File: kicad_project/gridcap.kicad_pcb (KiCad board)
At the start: 2 copper layers, 68 parts

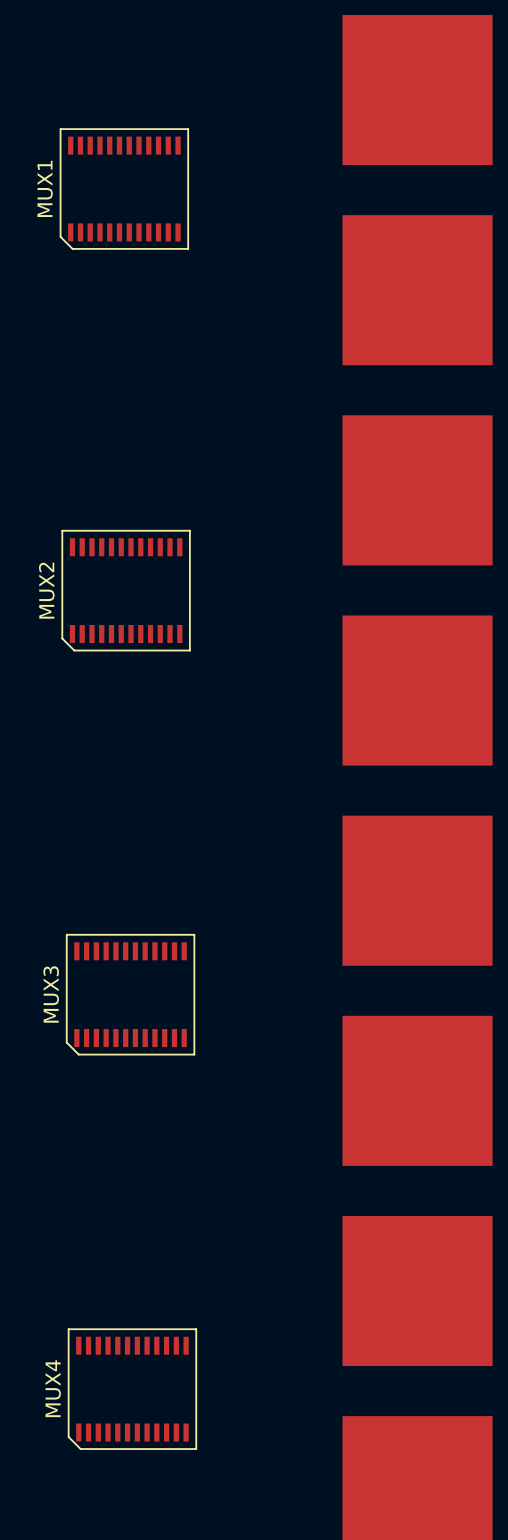
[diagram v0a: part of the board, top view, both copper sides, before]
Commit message: Fix pad pin number
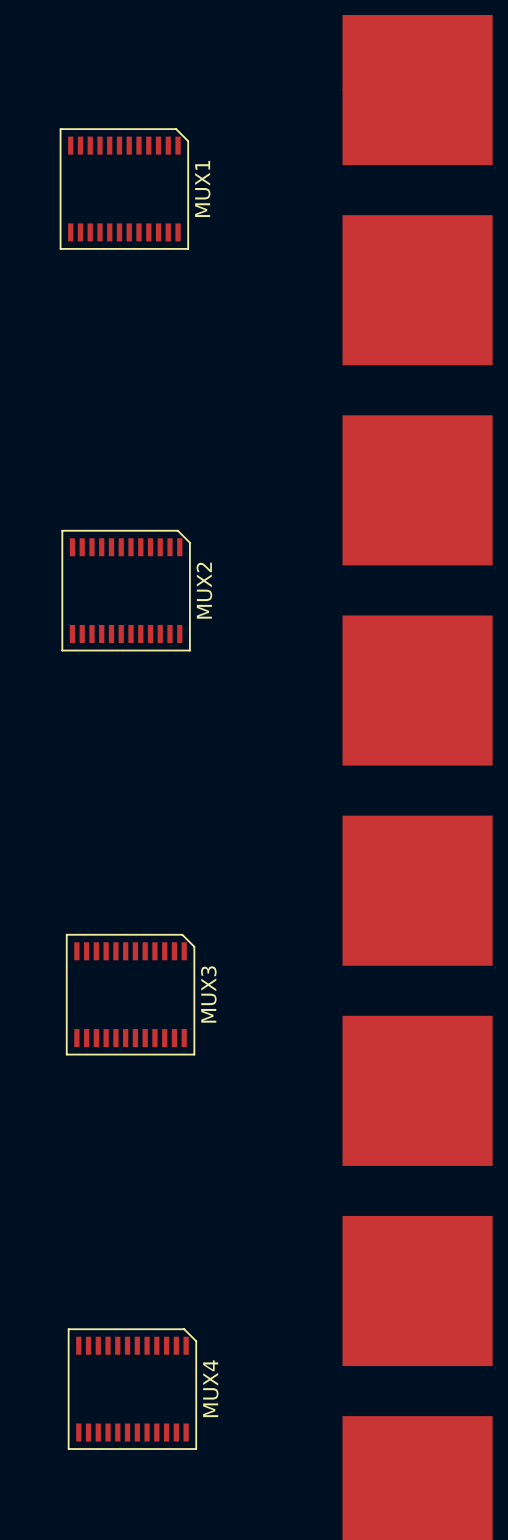
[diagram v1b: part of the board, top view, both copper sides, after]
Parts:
- turned MUX1 to 180 degrees
- turned MUX2 to 180 degrees
- turned MUX3 to 180 degrees
- turned MUX4 to 180 degrees
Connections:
- PAD1 pad 1: (no net) -> Net-(MUX1-Y7)
- PAD10 pad 1: (no net) -> Net-(MUX1-Y9)
- PAD11 pad 1: (no net) -> Net-(MUX1-Y10)
- PAD12 pad 1: (no net) -> Net-(MUX1-Y11)
- PAD13 pad 1: (no net) -> Net-(MUX1-Y12)
- PAD14 pad 1: (no net) -> Net-(MUX1-Y13)
- PAD15 pad 1: (no net) -> Net-(MUX1-Y14)
- PAD16 pad 1: (no net) -> Net-(MUX1-Y15)
- PAD17 pad 1: (no net) -> Net-(MUX2-Y7)
- PAD18 pad 1: (no net) -> Net-(MUX2-Y8)
- PAD19 pad 1: (no net) -> Net-(MUX2-Y6)
- PAD2 pad 1: (no net) -> Net-(MUX1-Y6)
- PAD20 pad 1: (no net) -> Net-(MUX2-Y9)
- PAD21 pad 1: (no net) -> Net-(MUX2-Y5)
- PAD22 pad 1: (no net) -> Net-(MUX2-Y10)
- PAD23 pad 1: (no net) -> Net-(MUX2-Y4)
- PAD24 pad 1: (no net) -> Net-(MUX2-Y11)
- PAD25 pad 1: (no net) -> Net-(MUX2-Y3)
- PAD26 pad 1: (no net) -> Net-(MUX2-Y12)
- PAD27 pad 1: (no net) -> Net-(MUX2-Y2)
- PAD28 pad 1: (no net) -> Net-(MUX2-Y13)
- PAD29 pad 1: (no net) -> Net-(MUX2-Y1)
- PAD3 pad 1: (no net) -> Net-(MUX1-Y5)
- PAD30 pad 1: (no net) -> Net-(MUX2-Y14)
- PAD31 pad 1: (no net) -> Net-(MUX2-Y0)
- PAD32 pad 1: (no net) -> Net-(MUX2-Y15)
- PAD33 pad 1: (no net) -> Net-(MUX3-Y7)
- PAD34 pad 1: (no net) -> Net-(MUX3-Y8)
- PAD35 pad 1: (no net) -> Net-(MUX3-Y6)
- PAD36 pad 1: (no net) -> Net-(MUX3-Y9)
- PAD37 pad 1: (no net) -> Net-(MUX3-Y5)
- PAD38 pad 1: (no net) -> Net-(MUX3-Y10)
- PAD39 pad 1: (no net) -> Net-(MUX3-Y4)
- PAD4 pad 1: (no net) -> Net-(MUX1-Y4)
- PAD40 pad 1: (no net) -> Net-(MUX3-Y11)
- PAD41 pad 1: (no net) -> Net-(MUX3-Y3)
- PAD42 pad 1: (no net) -> Net-(MUX3-Y12)
- PAD43 pad 1: (no net) -> Net-(MUX3-Y2)
- PAD44 pad 1: (no net) -> Net-(MUX3-Y13)
- PAD45 pad 1: (no net) -> Net-(MUX3-Y1)
- PAD46 pad 1: (no net) -> Net-(MUX3-Y14)
- PAD47 pad 1: (no net) -> Net-(MUX3-Y0)
- PAD48 pad 1: (no net) -> Net-(MUX3-Y15)
- PAD49 pad 1: (no net) -> Net-(MUX4-Y7)
- PAD5 pad 1: (no net) -> Net-(MUX1-Y3)
- PAD50 pad 1: (no net) -> Net-(MUX4-Y8)
- PAD51 pad 1: (no net) -> Net-(MUX4-Y6)
- PAD52 pad 1: (no net) -> Net-(MUX4-Y9)
- PAD53 pad 1: (no net) -> Net-(MUX4-Y5)
- PAD54 pad 1: (no net) -> Net-(MUX4-Y10)
- PAD55 pad 1: (no net) -> Net-(MUX4-Y4)
- PAD56 pad 1: (no net) -> Net-(MUX4-Y11)
- PAD57 pad 1: (no net) -> Net-(MUX4-Y3)
- PAD58 pad 1: (no net) -> Net-(MUX4-Y12)
- PAD59 pad 1: (no net) -> Net-(MUX4-Y2)
- PAD6 pad 1: (no net) -> Net-(MUX1-Y2)
- PAD60 pad 1: (no net) -> Net-(MUX4-Y13)
- PAD61 pad 1: (no net) -> Net-(MUX4-Y1)
- PAD62 pad 1: (no net) -> Net-(MUX4-Y14)
- PAD63 pad 1: (no net) -> Net-(MUX4-Y0)
- PAD64 pad 1: (no net) -> Net-(MUX4-Y15)
- PAD7 pad 1: (no net) -> Net-(MUX1-Y1)
- PAD8 pad 1: (no net) -> Net-(MUX1-Y0)
- PAD9 pad 1: (no net) -> Net-(MUX1-Y8)
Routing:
- net Net-(MUX1-Y7): track 0.00 -> 5.00 mm

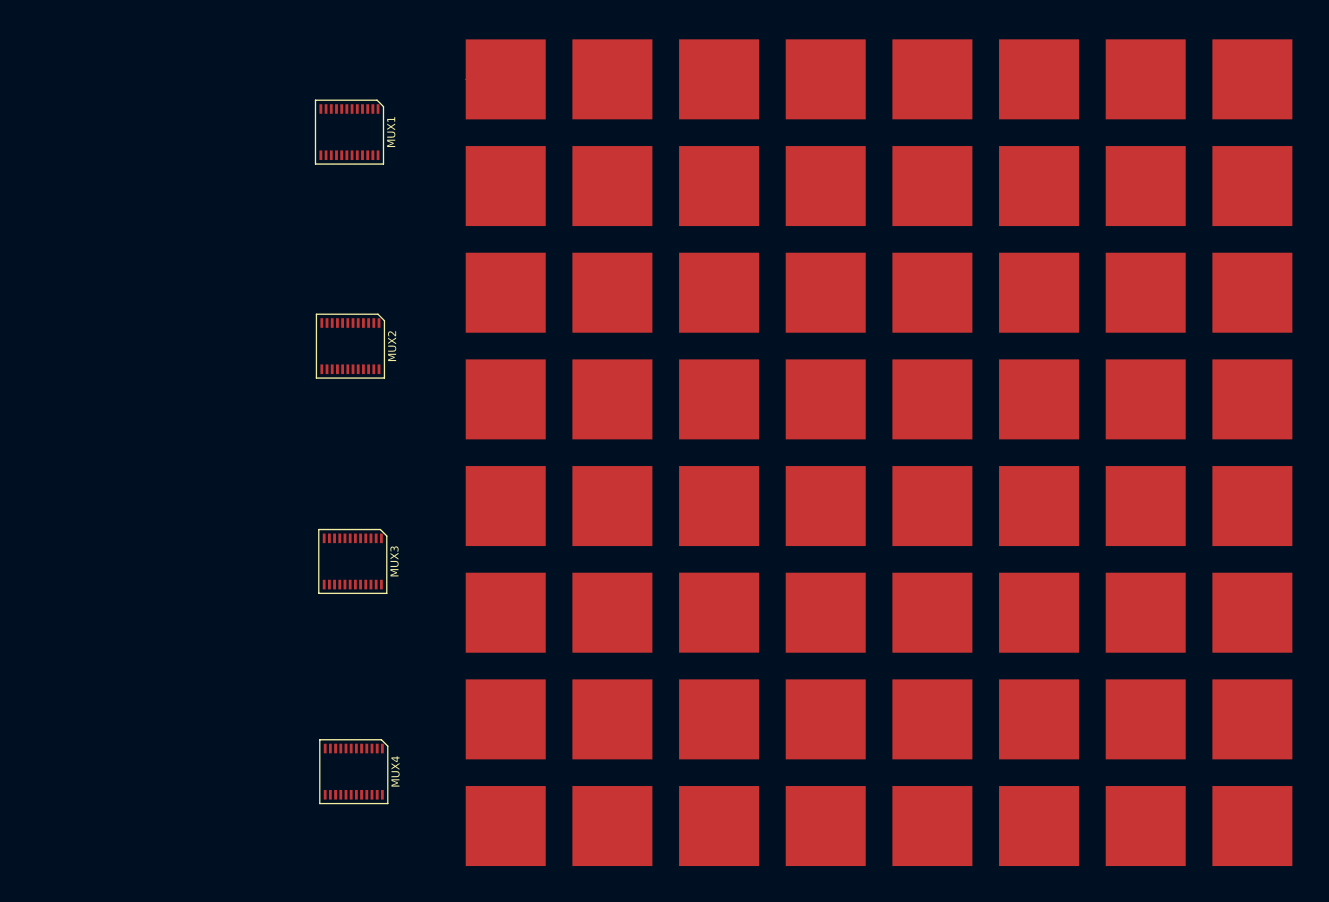
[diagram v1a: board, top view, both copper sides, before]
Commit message: Begin rewiring pads and muxes
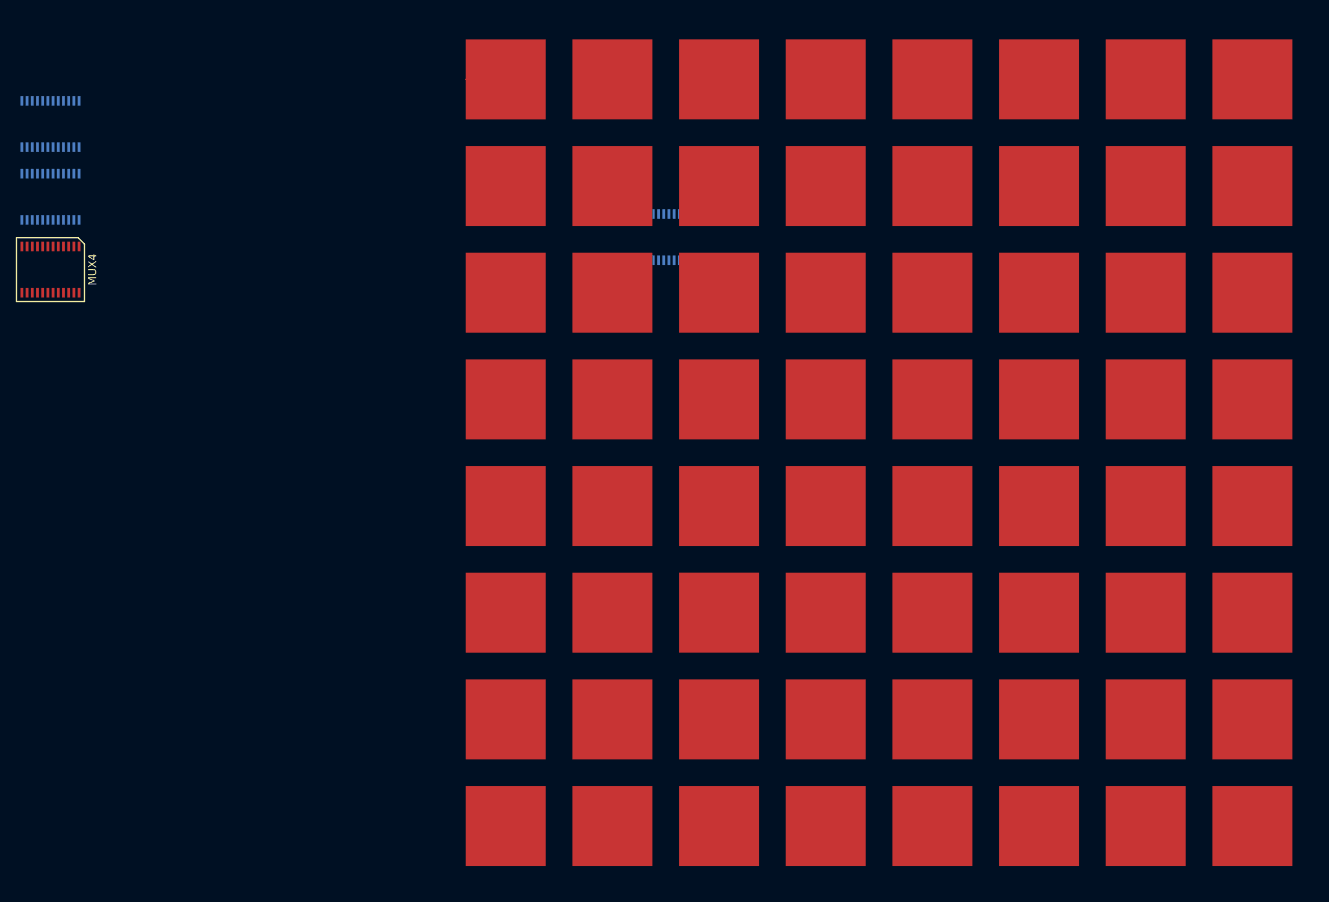
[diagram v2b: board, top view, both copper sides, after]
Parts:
- MUX1, MUX2, MUX3: moved to B.Cu
- moved MUX4 73.3 mm to (108.2, 77.1)
- moved MUX3 59.2 mm to (108.2, 68.0), turned to 0 degrees
- moved MUX2 46.7 mm to (108.2, 58.9), turned to 0 degrees
- moved MUX1 41.7 mm to (185.2, 73.1), turned to 0 degrees
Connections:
- MUX1 pad 12: (no net) -> GND
- MUX1 pad 24: (no net) -> unconnected-(MUX1-Vcc-Pad24)
- MUX2 pad 12: (no net) -> GND
- MUX2 pad 16: Net-(MUX2-Y15) -> unconnected-(MUX2-Y15-Pad16)
- MUX2 pad 17: Net-(MUX2-Y14) -> unconnected-(MUX2-Y14-Pad17)
- MUX2 pad 18: Net-(MUX2-Y13) -> unconnected-(MUX2-Y13-Pad18)
- MUX2 pad 19: Net-(MUX2-Y12) -> unconnected-(MUX2-Y12-Pad19)
- MUX2 pad 2: Net-(MUX2-Y7) -> unconnected-(MUX2-Y7-Pad2)
- MUX2 pad 20: Net-(MUX2-Y11) -> unconnected-(MUX2-Y11-Pad20)
- MUX2 pad 21: Net-(MUX2-Y10) -> unconnected-(MUX2-Y10-Pad21)
- MUX2 pad 22: Net-(MUX2-Y9) -> unconnected-(MUX2-Y9-Pad22)
- MUX2 pad 23: Net-(MUX2-Y8) -> unconnected-(MUX2-Y8-Pad23)
- MUX2 pad 24: (no net) -> unconnected-(MUX2-Vcc-Pad24)
- MUX2 pad 3: Net-(MUX2-Y6) -> unconnected-(MUX2-Y6-Pad3)
- MUX2 pad 4: Net-(MUX2-Y5) -> unconnected-(MUX2-Y5-Pad4)
- MUX2 pad 5: Net-(MUX2-Y4) -> unconnected-(MUX2-Y4-Pad5)
- MUX2 pad 6: Net-(MUX2-Y3) -> unconnected-(MUX2-Y3-Pad6)
- MUX2 pad 7: Net-(MUX2-Y2) -> unconnected-(MUX2-Y2-Pad7)
- MUX2 pad 8: Net-(MUX2-Y1) -> unconnected-(MUX2-Y1-Pad8)
- MUX2 pad 9: Net-(MUX2-Y0) -> unconnected-(MUX2-Y0-Pad9)
- MUX3 pad 12: (no net) -> GND
- MUX3 pad 16: Net-(MUX3-Y15) -> unconnected-(MUX3-Y15-Pad16)
- MUX3 pad 17: Net-(MUX3-Y14) -> unconnected-(MUX3-Y14-Pad17)
- MUX3 pad 18: Net-(MUX3-Y13) -> unconnected-(MUX3-Y13-Pad18)
- MUX3 pad 19: Net-(MUX3-Y12) -> unconnected-(MUX3-Y12-Pad19)
- MUX3 pad 2: Net-(MUX3-Y7) -> unconnected-(MUX3-Y7-Pad2)
- MUX3 pad 20: Net-(MUX3-Y11) -> unconnected-(MUX3-Y11-Pad20)
- MUX3 pad 21: Net-(MUX3-Y10) -> unconnected-(MUX3-Y10-Pad21)
- MUX3 pad 22: Net-(MUX3-Y9) -> unconnected-(MUX3-Y9-Pad22)
- MUX3 pad 23: Net-(MUX3-Y8) -> unconnected-(MUX3-Y8-Pad23)
- MUX3 pad 24: (no net) -> unconnected-(MUX3-Vcc-Pad24)
- MUX3 pad 3: Net-(MUX3-Y6) -> unconnected-(MUX3-Y6-Pad3)
- MUX3 pad 4: Net-(MUX3-Y5) -> unconnected-(MUX3-Y5-Pad4)
- MUX3 pad 5: Net-(MUX3-Y4) -> unconnected-(MUX3-Y4-Pad5)
- MUX3 pad 6: Net-(MUX3-Y3) -> unconnected-(MUX3-Y3-Pad6)
- MUX3 pad 7: Net-(MUX3-Y2) -> unconnected-(MUX3-Y2-Pad7)
- MUX3 pad 8: Net-(MUX3-Y1) -> unconnected-(MUX3-Y1-Pad8)
- MUX3 pad 9: Net-(MUX3-Y0) -> unconnected-(MUX3-Y0-Pad9)
- MUX4 pad 12: (no net) -> GND
- MUX4 pad 16: Net-(MUX4-Y15) -> unconnected-(MUX4-Y15-Pad16)
- MUX4 pad 17: Net-(MUX4-Y14) -> unconnected-(MUX4-Y14-Pad17)
- MUX4 pad 18: Net-(MUX4-Y13) -> unconnected-(MUX4-Y13-Pad18)
- MUX4 pad 19: Net-(MUX4-Y12) -> unconnected-(MUX4-Y12-Pad19)
- MUX4 pad 2: Net-(MUX4-Y7) -> unconnected-(MUX4-Y7-Pad2)
- MUX4 pad 20: Net-(MUX4-Y11) -> unconnected-(MUX4-Y11-Pad20)
- MUX4 pad 21: Net-(MUX4-Y10) -> unconnected-(MUX4-Y10-Pad21)
- MUX4 pad 22: Net-(MUX4-Y9) -> unconnected-(MUX4-Y9-Pad22)
- MUX4 pad 23: Net-(MUX4-Y8) -> unconnected-(MUX4-Y8-Pad23)
- MUX4 pad 24: (no net) -> unconnected-(MUX4-Vcc-Pad24)
- MUX4 pad 3: Net-(MUX4-Y6) -> unconnected-(MUX4-Y6-Pad3)
- MUX4 pad 4: Net-(MUX4-Y5) -> unconnected-(MUX4-Y5-Pad4)
- MUX4 pad 5: Net-(MUX4-Y4) -> unconnected-(MUX4-Y4-Pad5)
- MUX4 pad 6: Net-(MUX4-Y3) -> unconnected-(MUX4-Y3-Pad6)
- MUX4 pad 7: Net-(MUX4-Y2) -> unconnected-(MUX4-Y2-Pad7)
- MUX4 pad 8: Net-(MUX4-Y1) -> unconnected-(MUX4-Y1-Pad8)
- MUX4 pad 9: Net-(MUX4-Y0) -> unconnected-(MUX4-Y0-Pad9)
- PAD1 pad 1: Net-(MUX1-Y7) -> Net-(MUX1-Y6)
- PAD10 pad 1: Net-(MUX1-Y9) -> Net-(MUX1-Y5)
- PAD11 pad 1: Net-(MUX1-Y10) -> Net-(MUX1-Y2)
- PAD12 pad 1: Net-(MUX1-Y11) -> Net-(MUX1-Y0)
- PAD13 pad 1: Net-(MUX1-Y12) -> unconnected-(PAD13-Pad1)
- PAD14 pad 1: Net-(MUX1-Y13) -> unconnected-(PAD14-Pad1)
- PAD15 pad 1: Net-(MUX1-Y14) -> unconnected-(PAD15-Pad1)
- PAD16 pad 1: Net-(MUX1-Y15) -> unconnected-(PAD16-Pad1)
- PAD17 pad 1: Net-(MUX2-Y7) -> Net-(MUX1-Y8)
- PAD18 pad 1: Net-(MUX2-Y8) -> Net-(MUX1-Y10)
- PAD19 pad 1: Net-(MUX2-Y6) -> Net-(MUX1-Y13)
- PAD2 pad 1: Net-(MUX1-Y6) -> Net-(MUX1-Y4)
- PAD20 pad 1: Net-(MUX2-Y9) -> Net-(MUX1-Y15)
- PAD21 pad 1: Net-(MUX2-Y5) -> unconnected-(PAD21-Pad1)
- PAD22 pad 1: Net-(MUX2-Y10) -> unconnected-(PAD22-Pad1)
- PAD23 pad 1: Net-(MUX2-Y4) -> unconnected-(PAD23-Pad1)
- PAD24 pad 1: Net-(MUX2-Y11) -> unconnected-(PAD24-Pad1)
- PAD25 pad 1: Net-(MUX2-Y3) -> Net-(MUX1-Y9)
- PAD26 pad 1: Net-(MUX2-Y12) -> Net-(MUX1-Y11)
- PAD27 pad 1: Net-(MUX2-Y2) -> Net-(MUX1-Y12)
- PAD28 pad 1: Net-(MUX2-Y13) -> Net-(MUX1-Y14)
- PAD29 pad 1: Net-(MUX2-Y1) -> unconnected-(PAD29-Pad1)
- PAD3 pad 1: Net-(MUX1-Y5) -> Net-(MUX1-Y3)
- PAD30 pad 1: Net-(MUX2-Y14) -> unconnected-(PAD30-Pad1)
- PAD31 pad 1: Net-(MUX2-Y0) -> unconnected-(PAD31-Pad1)
- PAD32 pad 1: Net-(MUX2-Y15) -> unconnected-(PAD32-Pad1)
- PAD33 pad 1: Net-(MUX3-Y7) -> unconnected-(PAD33-Pad1)
- PAD34 pad 1: Net-(MUX3-Y8) -> unconnected-(PAD34-Pad1)
- PAD35 pad 1: Net-(MUX3-Y6) -> unconnected-(PAD35-Pad1)
- PAD36 pad 1: Net-(MUX3-Y9) -> unconnected-(PAD36-Pad1)
- PAD37 pad 1: Net-(MUX3-Y5) -> unconnected-(PAD37-Pad1)
- PAD38 pad 1: Net-(MUX3-Y10) -> unconnected-(PAD38-Pad1)
- PAD39 pad 1: Net-(MUX3-Y4) -> unconnected-(PAD39-Pad1)
- PAD4 pad 1: Net-(MUX1-Y4) -> Net-(MUX1-Y1)
- PAD40 pad 1: Net-(MUX3-Y11) -> unconnected-(PAD40-Pad1)
- PAD41 pad 1: Net-(MUX3-Y3) -> unconnected-(PAD41-Pad1)
- PAD42 pad 1: Net-(MUX3-Y12) -> unconnected-(PAD42-Pad1)
- PAD43 pad 1: Net-(MUX3-Y2) -> unconnected-(PAD43-Pad1)
- PAD44 pad 1: Net-(MUX3-Y13) -> unconnected-(PAD44-Pad1)
- PAD45 pad 1: Net-(MUX3-Y1) -> unconnected-(PAD45-Pad1)
- PAD46 pad 1: Net-(MUX3-Y14) -> unconnected-(PAD46-Pad1)
- PAD47 pad 1: Net-(MUX3-Y0) -> unconnected-(PAD47-Pad1)
- PAD48 pad 1: Net-(MUX3-Y15) -> unconnected-(PAD48-Pad1)
- PAD49 pad 1: Net-(MUX4-Y7) -> unconnected-(PAD49-Pad1)
- PAD5 pad 1: Net-(MUX1-Y3) -> unconnected-(PAD5-Pad1)
- PAD50 pad 1: Net-(MUX4-Y8) -> unconnected-(PAD50-Pad1)
- PAD51 pad 1: Net-(MUX4-Y6) -> unconnected-(PAD51-Pad1)
- PAD52 pad 1: Net-(MUX4-Y9) -> unconnected-(PAD52-Pad1)
- PAD53 pad 1: Net-(MUX4-Y5) -> unconnected-(PAD53-Pad1)
- PAD54 pad 1: Net-(MUX4-Y10) -> unconnected-(PAD54-Pad1)
- PAD55 pad 1: Net-(MUX4-Y4) -> unconnected-(PAD55-Pad1)
- PAD56 pad 1: Net-(MUX4-Y11) -> unconnected-(PAD56-Pad1)
- PAD57 pad 1: Net-(MUX4-Y3) -> unconnected-(PAD57-Pad1)
- PAD58 pad 1: Net-(MUX4-Y12) -> unconnected-(PAD58-Pad1)
- PAD59 pad 1: Net-(MUX4-Y2) -> unconnected-(PAD59-Pad1)
- PAD6 pad 1: Net-(MUX1-Y2) -> unconnected-(PAD6-Pad1)
- PAD60 pad 1: Net-(MUX4-Y13) -> unconnected-(PAD60-Pad1)
- PAD61 pad 1: Net-(MUX4-Y1) -> unconnected-(PAD61-Pad1)
- PAD62 pad 1: Net-(MUX4-Y14) -> unconnected-(PAD62-Pad1)
- PAD63 pad 1: Net-(MUX4-Y0) -> unconnected-(PAD63-Pad1)
- PAD64 pad 1: Net-(MUX4-Y15) -> unconnected-(PAD64-Pad1)
- PAD7 pad 1: Net-(MUX1-Y1) -> unconnected-(PAD7-Pad1)
- PAD8 pad 1: Net-(MUX1-Y0) -> unconnected-(PAD8-Pad1)
- PAD9 pad 1: Net-(MUX1-Y8) -> Net-(MUX1-Y7)
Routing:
- net Net-(MUX1-Y7): track 5.00 -> 0.00 mm
- net Net-(MUX1-Y6): track 0.00 -> 5.00 mm
